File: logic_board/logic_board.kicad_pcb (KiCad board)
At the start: 4 copper layers, 80 x 30 mm, 55 parts, among them J1 Debug, J2 Audio In, J3 SJ2-3595X-SMT, J4 Amphenol 124015, J5 Batt, SW1 TL3315NF160Q, SW2 TL3315NF160Q, SW3 TL3315NF160Q, SW4 TL3315NF160Q, SW5 Power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

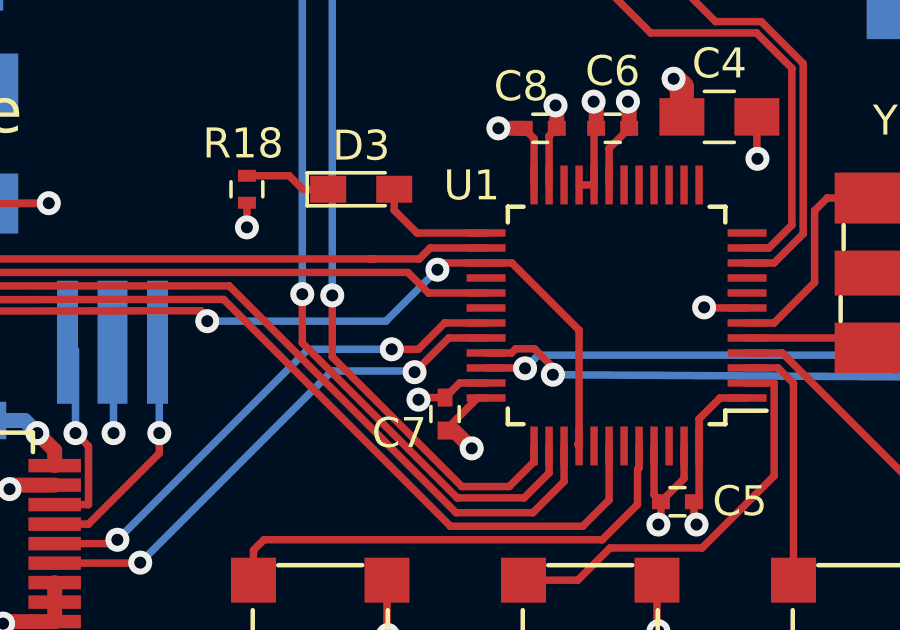
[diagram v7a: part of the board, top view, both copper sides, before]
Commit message: Leave a small via connected to pin PA8.
There is a contradiction in the datasheet between two tables. I've taken an educated guess,
but if that is wrong, this will make it easier to rework.
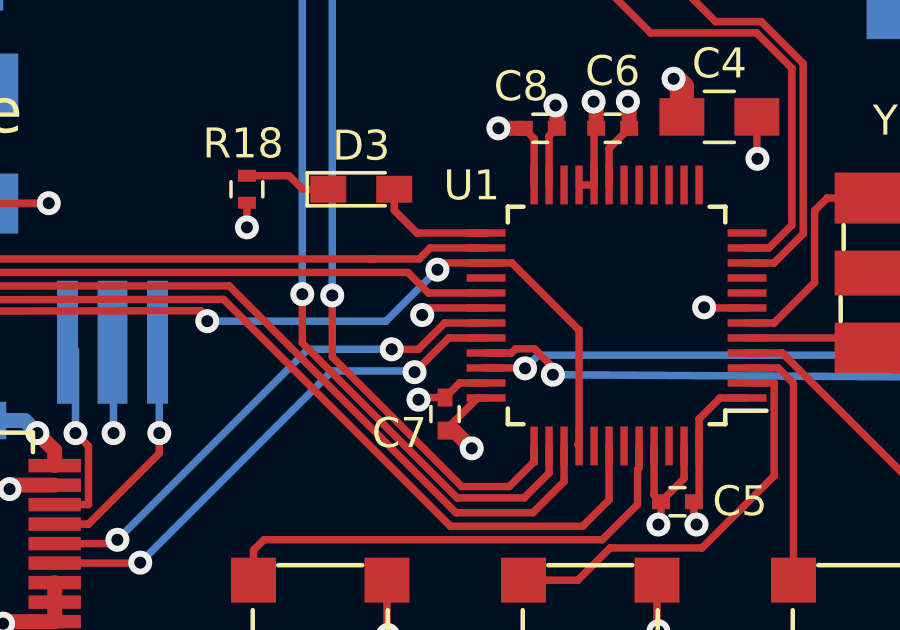
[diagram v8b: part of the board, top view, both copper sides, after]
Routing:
- net Net-(U1-Pad30): track 0.00 -> 2.23 mm, vias 0 -> 1
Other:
- board text added: "RX"
- board text added: "TX"
- board text removed: "SRX"
- board text removed: "STX"
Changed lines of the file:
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@@
     (thickness 1.6)
     (drawings 21)
-    (tracks 546)
+    (tracks 549)
     (zones 0)
     (modules 55)
@@
       (usegerberadvancedattributes false)
       (creategerberjobfile false)
-      (excludeedgelayer true)
+      (excludeedgelayer false)
       (linewidth 0.150000)
       (plotframeref false)
       (viasonmask false)
       (mode 1)
-      (useauxorigin true)
+      (useauxorigin false)
       (hpglpennumber 1)
       (hpglpenspeed 20)
@@
     (effects (font (size 0.75 0.75) (thickness 0.125)) (justify left mirror))
   )
-  (gr_text SRX (at 141.859 103.632 90) (layer B.SilkS)
+  (gr_text RX (at 141.859 103.632 90) (layer B.SilkS)
     (effects (font (size 0.75 0.75) (thickness 0.125)) (justify left mirror))
   )
-  (gr_text STX (at 144.145 103.632 90) (layer B.SilkS)
+  (gr_text TX (at 144.145 103.632 90) (layer B.SilkS)
     (effects (font (size 0.75 0.75) (thickness 0.125)) (justify left mirror))
   )
@@
   (segment (start 136.22224 110.67624) (end 135.466 109.92) (width 0.25) (layer F.Cu) (net 66))
   (segment (start 138.52754 110.67624) (end 136.22224 110.67624) (width 0.25) (layer F.Cu) (net 66) (status 10))
+  (via (at 136.398 113.411) (size 0.8) (drill 0.4) (layers F.Cu B.Cu) (net 67))
+  (segment (start 136.63276 113.17624) (end 136.398 113.411) (width 0.25) (layer F.Cu) (net 67))
+  (segment (start 138.52754 113.17624) (end 136.63276 113.17624) (width 0.25) (layer F.Cu) (net 67))
   (segment (start 147.956142 111.17624) (end 148.72099 110.411392) (width 0.25) (layer F.Cu) (net 69))
   (segment (start 147.22754 111.17624) (end 147.956142 111.17624) (width 0.25) (layer F.Cu) (net 69) (status 10))
